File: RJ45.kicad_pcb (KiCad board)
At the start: 2 copper layers, 3 parts, among them J1 Conn_01x06, J2 RJ45_Amphenol_RJMG1BD3B8K1ANR, J3 Conn_01x06

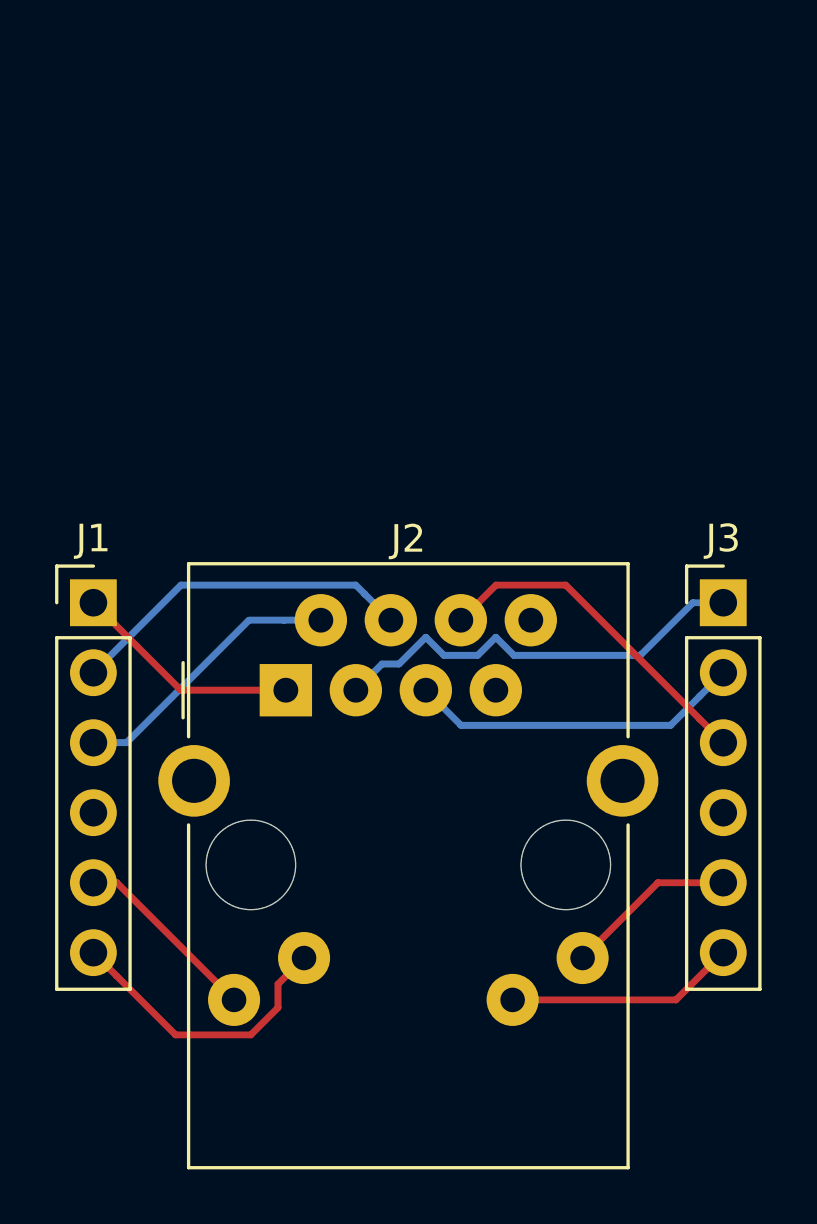
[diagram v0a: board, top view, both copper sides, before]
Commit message: Rearrange to make narrower.
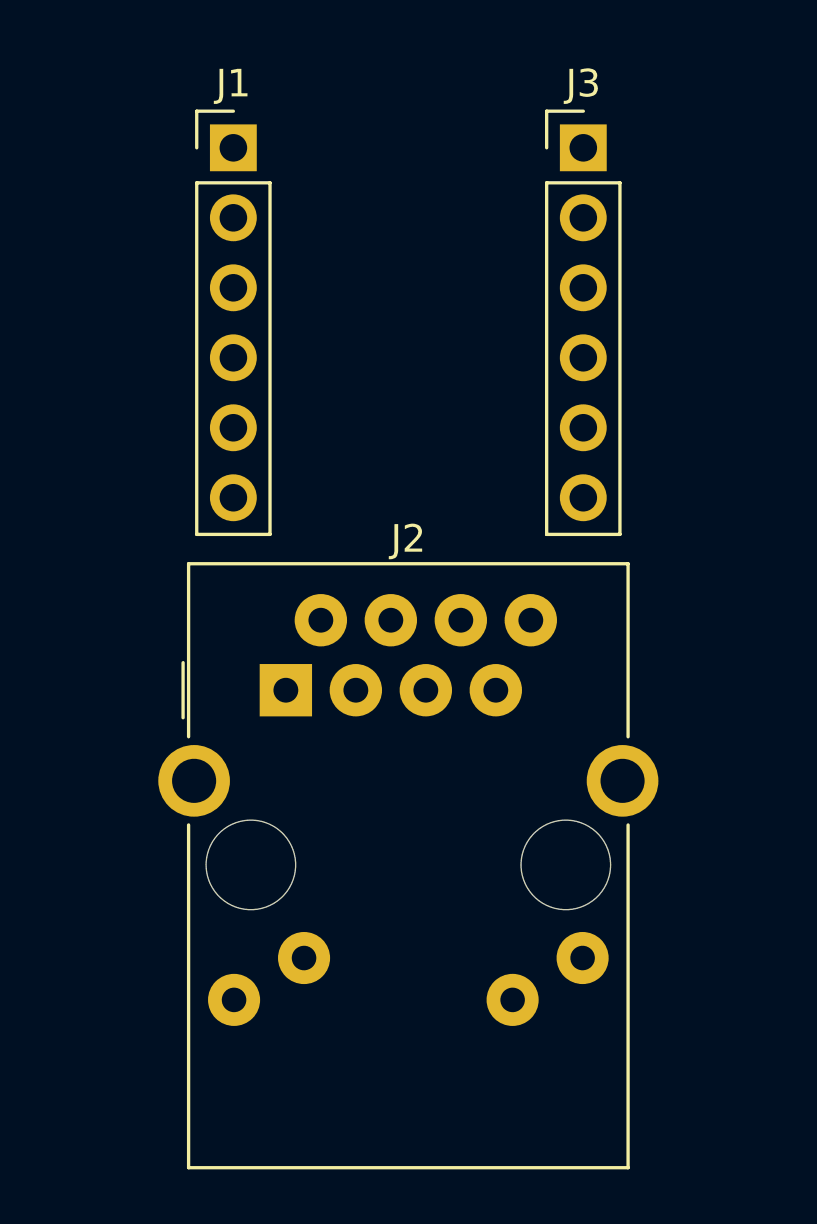
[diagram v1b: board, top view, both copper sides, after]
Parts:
- moved J1 17.3 mm to (132.1, 77.5)
- moved J3 17.3 mm to (144.8, 77.5)
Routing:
- net Net-(J2-PadR3): track 15.7 -> 0.00 mm
- net Net-(J1-Pad2): track 12.6 -> 0.00 mm
- net Net-(J2-PadR6): track 12.4 -> 0.00 mm
- net Net-(J2-PadR5): track 12.1 -> 0.00 mm
- net Net-(J1-Pad6): track 10.5 -> 0.00 mm
- net Net-(J1-Pad3): track 10.1 -> 0.00 mm
- net Net-(J2-PadL2): track 8.36 -> 0.00 mm
- net Net-(J1-Pad1): track 8.30 -> 0.00 mm
- net Net-(J1-Pad5): track 6.87 -> 0.00 mm
- net Net-(J2-PadL1): track 6.24 -> 0.00 mm
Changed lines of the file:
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@@
     (thickness 1.6)
     (drawings 0)
-    (tracks 40)
+    (tracks 0)
     (zones 0)
     (modules 3)
@@
     (pad_to_mask_clearance 0)
     (aux_axis_origin 0 0)
-    (visible_elements FFFFE77F)
+    (visible_elements FFFFF77F)
     (pcbplotparams
       (layerselection 0x00030_80000001)
@@
   )
   (module Pin_Headers:Pin_Header_Straight_1x06_Pitch2.54mm (layer F.Cu)
-    (at 127 93.98)
+    (at 132.08 77.47)
     (descr "Through hole straight pin header, 1x06, 2.54mm pitch, single row")
     (tags "Through hole pin header THT 1x06 2.54mm single row")
@@
   )
   (module Pin_Headers:Pin_Header_Straight_1x06_Pitch2.54mm (layer F.Cu)
-    (at 149.86 93.98)
+    (at 144.78 77.47)
     (descr "Through hole straight pin header, 1x06, 2.54mm pitch, single row")
     (tags "Through hole pin header THT 1x06 2.54mm single row")
@@
     )
   )
-  (segment (start 133.985 97.155) (end 130.175 97.155) (width 0.25) (layer F.Cu) (net 1))
-  (segment (start 130.175 97.155) (end 127 93.98) (width 0.25) (layer F.Cu) (net 1))
-  (segment (start 127 96.52) (end 130.180001 93.339999) (width 0.25) (layer B.Cu) (net 2))
-  (segment (start 130.180001 93.339999) (end 136.519999 93.339999) (width 0.25) (layer B.Cu) (net 2))
-  (segment (start 136.519999 93.339999) (end 136.845001 93.665001) (width 0.25) (layer B.Cu) (net 2))
-  (segment (start 136.845001 93.665001) (end 137.795 94.615) (width 0.25) (layer B.Cu) (net 2))
-  (segment (start 127 99.06) (end 128.202081 99.06) (width 0.25) (layer B.Cu) (net 3))
-  (segment (start 128.202081 99.06) (end 132.647081 94.615) (width 0.25) (layer B.Cu) (net 3))
-  (segment (start 132.647081 94.615) (end 133.911498 94.615) (width 0.25) (layer B.Cu) (net 3))
-  (segment (start 133.911498 94.615) (end 135.255 94.615) (width 0.25) (layer B.Cu) (net 3))
-  (segment (start 132.105 108.395) (end 127.85 104.14) (width 0.25) (layer F.Cu) (net 5))
-  (segment (start 127.85 104.14) (end 127 104.14) (width 0.25) (layer F.Cu) (net 5))
-  (segment (start 134.645 106.875) (end 133.700001 107.819999) (width 0.25) (layer F.Cu) (net 6))
-  (segment (start 133.700001 107.819999) (end 133.700001 108.679601) (width 0.25) (layer F.Cu) (net 6))
-  (segment (start 133.700001 108.679601) (end 132.714601 109.665001) (width 0.25) (layer F.Cu) (net 6))
-  (segment (start 132.714601 109.665001) (end 129.985001 109.665001) (width 0.25) (layer F.Cu) (net 6))
-  (segment (start 129.985001 109.665001) (end 127.849999 107.529999) (width 0.25) (layer F.Cu) (net 6))
-  (segment (start 127.849999 107.529999) (end 127 106.68) (width 0.25) (layer F.Cu) (net 6))
-  (segment (start 136.525 97.155) (end 137.474999 96.205001) (width 0.25) (layer B.Cu) (net 7))
-  (segment (start 137.474999 96.205001) (end 138.092001 96.205001) (width 0.25) (layer B.Cu) (net 7))
-  (segment (start 138.092001 96.205001) (end 139.065 95.232002) (width 0.25) (layer B.Cu) (net 7))
-  (segment (start 139.065 95.232002) (end 139.722999 95.890001) (width 0.25) (layer B.Cu) (net 7))
-  (segment (start 139.722999 95.890001) (end 140.947001 95.890001) (width 0.25) (layer B.Cu) (net 7))
-  (segment (start 140.947001 95.890001) (end 141.605 95.232002) (width 0.25) (layer B.Cu) (net 7))
-  (segment (start 141.605 95.232002) (end 142.262999 95.890001) (width 0.25) (layer B.Cu) (net 7))
-  (segment (start 142.262999 95.890001) (end 146.849999 95.890001) (width 0.25) (layer B.Cu) (net 7))
-  (segment (start 146.849999 95.890001) (end 148.76 93.98) (width 0.25) (layer B.Cu) (net 7))
-  (segment (start 148.76 93.98) (end 149.86 93.98) (width 0.25) (layer B.Cu) (net 7))
-  (segment (start 139.065 97.155) (end 140.340001 98.430001) (width 0.25) (layer B.Cu) (net 8))
-  (segment (start 140.340001 98.430001) (end 147.949999 98.430001) (width 0.25) (layer B.Cu) (net 8))
-  (segment (start 147.949999 98.430001) (end 149.010001 97.369999) (width 0.25) (layer B.Cu) (net 8))
-  (segment (start 149.010001 97.369999) (end 149.86 96.52) (width 0.25) (layer B.Cu) (net 8))
-  (segment (start 140.335 94.615) (end 141.610001 93.339999) (width 0.25) (layer F.Cu) (net 9))
-  (segment (start 141.610001 93.339999) (end 144.139999 93.339999) (width 0.25) (layer F.Cu) (net 9))
-  (segment (start 144.139999 93.339999) (end 149.010001 98.210001) (width 0.25) (layer F.Cu) (net 9))
-  (segment (start 149.010001 98.210001) (end 149.86 99.06) (width 0.25) (layer F.Cu) (net 9))
-  (segment (start 144.755 106.875) (end 147.49 104.14) (width 0.25) (layer F.Cu) (net 12))
-  (segment (start 147.49 104.14) (end 149.86 104.14) (width 0.25) (layer F.Cu) (net 12))
-  (segment (start 142.215 108.395) (end 148.145 108.395) (width 0.25) (layer F.Cu) (net 13))
-  (segment (start 148.145 108.395) (end 149.86 106.68) (width 0.25) (layer F.Cu) (net 13))
 )

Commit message: Draw board outline.
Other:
- board outline added: 19.1 x 34.9 mm
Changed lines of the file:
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@@
     (area 0 0 0 0)
     (thickness 1.6)
-    (drawings 0)
+    (drawings 8)
     (tracks 0)
     (zones 0)
@@
     )
   )
+  (gr_line (start 128.905 92.075) (end 128.905 110.49) (angle 90) (layer Edge.Cuts) (width 0.15))
+  (gr_line (start 130.175 92.075) (end 128.905 92.075) (angle 90) (layer Edge.Cuts) (width 0.15))
+  (gr_line (start 130.175 75.565) (end 130.175 92.075) (angle 90) (layer Edge.Cuts) (width 0.15))
+  (gr_line (start 146.685 75.565) (end 130.175 75.565) (angle 90) (layer Edge.Cuts) (width 0.15))
+  (gr_line (start 146.685 92.075) (end 146.685 75.565) (angle 90) (layer Edge.Cuts) (width 0.15))
+  (gr_line (start 147.955 92.075) (end 146.685 92.075) (angle 90) (layer Edge.Cuts) (width 0.15))
+  (gr_line (start 147.955 110.49) (end 147.955 92.075) (angle 90) (layer Edge.Cuts) (width 0.15))
+  (gr_line (start 128.905 110.49) (end 147.955 110.49) (angle 90) (layer Edge.Cuts) (width 0.15))
 )

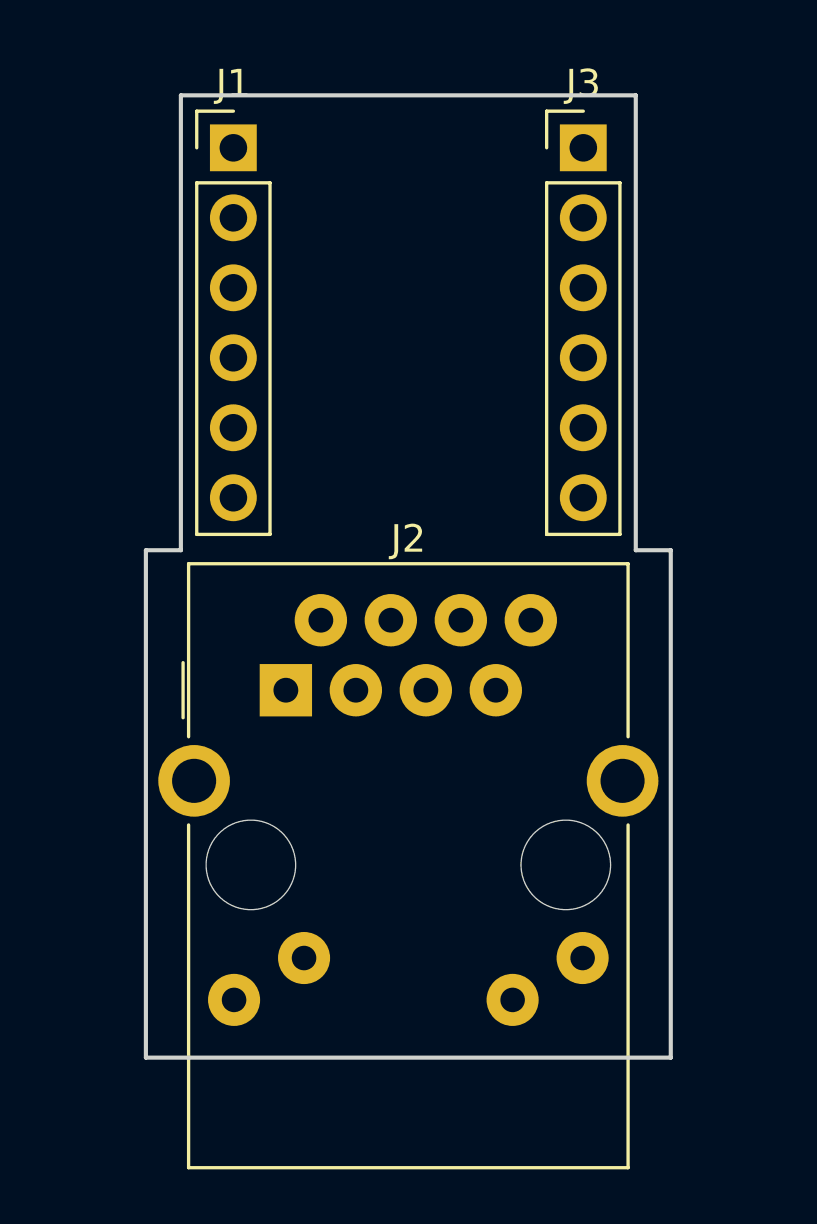
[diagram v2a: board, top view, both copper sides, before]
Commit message: Label pins on silkscreen.
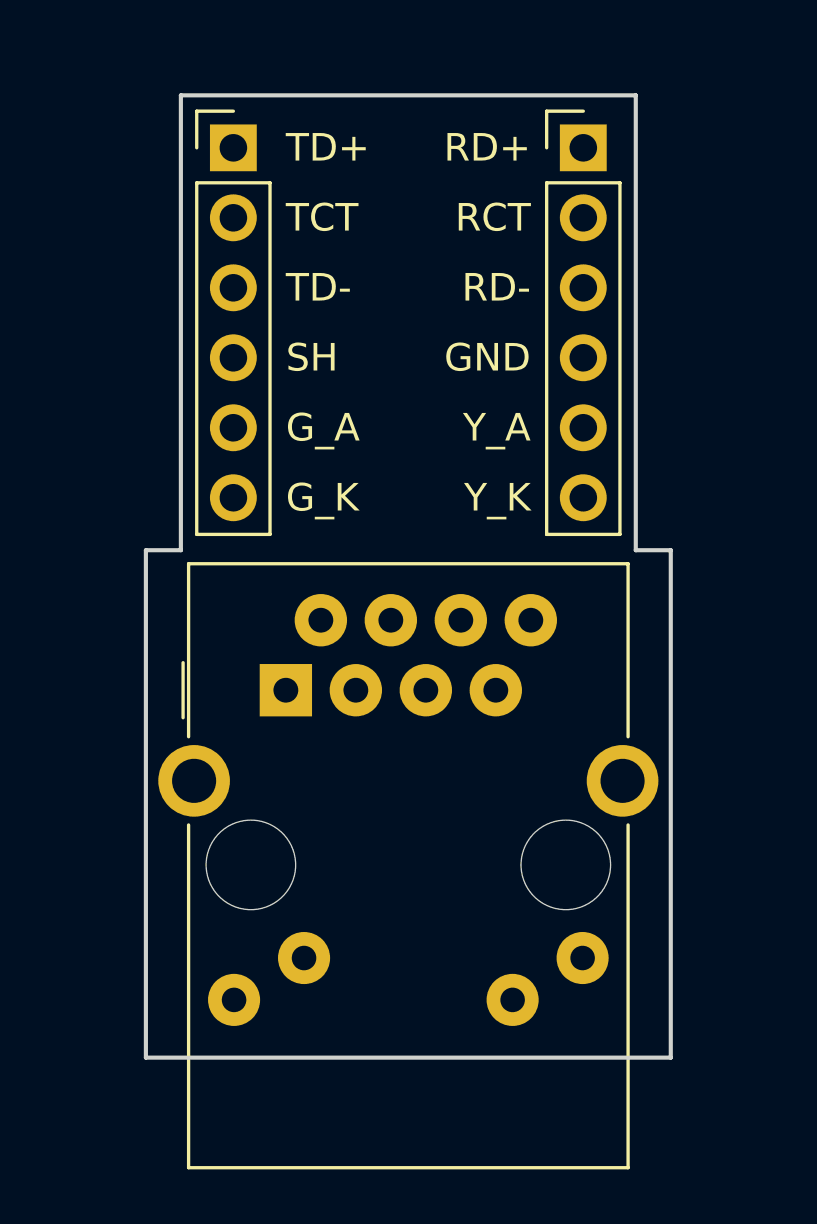
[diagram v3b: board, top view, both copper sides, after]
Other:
- board text added: "GND"
- board text added: "G_A"
- board text added: "G_K"
- board text added: "RCT"
- board text added: "RD+"
- board text added: "RD-"
- board text added: "SH"
- board text added: "TCT"
- board text added: "TD+"
- board text added: "TD-"
- board text added: "Y_A"
- board text added: "Y_K"
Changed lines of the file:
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@@
     (area 0 0 0 0)
     (thickness 1.6)
-    (drawings 8)
+    (drawings 20)
     (tracks 0)
     (zones 0)
@@
     (pad_to_mask_clearance 0)
     (aux_axis_origin 0 0)
-    (visible_elements FFFFF77F)
+    (visible_elements FFFEF77F)
     (pcbplotparams
       (layerselection 0x00030_80000001)
@@
     (descr "Through hole straight pin header, 1x06, 2.54mm pitch, single row")
     (tags "Through hole pin header THT 1x06 2.54mm single row")
-    (fp_text reference J1 (at 0 -2.33) (layer F.SilkS)
+    (fp_text reference J1 (at 0 -2.33) (layer F.SilkS) hide
       (effects (font (size 1 1) (thickness 0.15)))
     )
@@
     (descr "1 Port RJ45 Magjack Connector Through Hole 10/100 Base-T, AutoMDIX, https://www.amphenolcanada.com/ProductSearch/Drawings/AC/RJMG1BD3B8K1ANR.PDF")
     (tags "RJ45 Magjack")
-    (fp_text reference J2 (at 4.445 -5.49) (layer F.SilkS)
+    (fp_text reference J2 (at 4.445 -5.49) (layer F.SilkS) hide
       (effects (font (size 1 1) (thickness 0.15)))
     )
@@
     (descr "Through hole straight pin header, 1x06, 2.54mm pitch, single row")
     (tags "Through hole pin header THT 1x06 2.54mm single row")
-    (fp_text reference J3 (at 0 -2.33) (layer F.SilkS)
+    (fp_text reference J3 (at 0 -2.33) (layer F.SilkS) hide
       (effects (font (size 1 1) (thickness 0.15)))
     )
@@
     )
   )
+  (gr_text Y_K (at 142.875 90.17) (layer F.SilkS)
+    (effects (font (size 1 1) (thickness 0.2)) (justify right))
+  )
+  (gr_text Y_A (at 142.875 87.63) (layer F.SilkS)
+    (effects (font (size 1 1) (thickness 0.2)) (justify right))
+  )
+  (gr_text GND (at 142.875 85.09) (layer F.SilkS)
+    (effects (font (size 1 1) (thickness 0.2)) (justify right))
+  )
+  (gr_text RD- (at 142.875 82.55) (layer F.SilkS)
+    (effects (font (size 1 1) (thickness 0.2)) (justify right))
+  )
+  (gr_text RCT (at 142.875 80.01) (layer F.SilkS)
+    (effects (font (size 1 1) (thickness 0.2)) (justify right))
+  )
+  (gr_text RD+ (at 142.875 77.47) (layer F.SilkS)
+    (effects (font (size 1 1) (thickness 0.2)) (justify right))
+  )
+  (gr_text G_K (at 133.985 90.17) (layer F.SilkS)
+    (effects (font (size 1 1) (thickness 0.2)) (justify left))
+  )
+  (gr_text G_A (at 133.985 87.63) (layer F.SilkS)
+    (effects (font (size 1 1) (thickness 0.2)) (justify left))
+  )
+  (gr_text SH (at 133.985 85.09) (layer F.SilkS)
+    (effects (font (size 1 1) (thickness 0.2)) (justify left))
+  )
+  (gr_text TD- (at 133.985 82.55) (layer F.SilkS)
+    (effects (font (size 1 1) (thickness 0.2)) (justify left))
+  )
+  (gr_text TCT (at 133.985 80.01) (layer F.SilkS)
+    (effects (font (size 1 1) (thickness 0.2)) (justify left))
+  )
+  (gr_text TD+ (at 133.985 77.47) (layer F.SilkS)
+    (effects (font (size 1 1) (thickness 0.2)) (justify left))
+  )
   (gr_line (start 128.905 92.075) (end 128.905 110.49) (angle 90) (layer Edge.Cuts) (width 0.15))
